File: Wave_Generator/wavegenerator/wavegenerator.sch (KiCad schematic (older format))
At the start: 59 parts, among them J1 01x05, J2 USB_B_Micro, J3 Conn_Coaxial, J4 1x2Pinheader, SW1 button, SW2 button, SW3 SP3T, U1 ATmega328P-AU, U101 AZ1117E-3.3, U102 MC33063AD, U2 MAX038CPP, Y101 16MHz

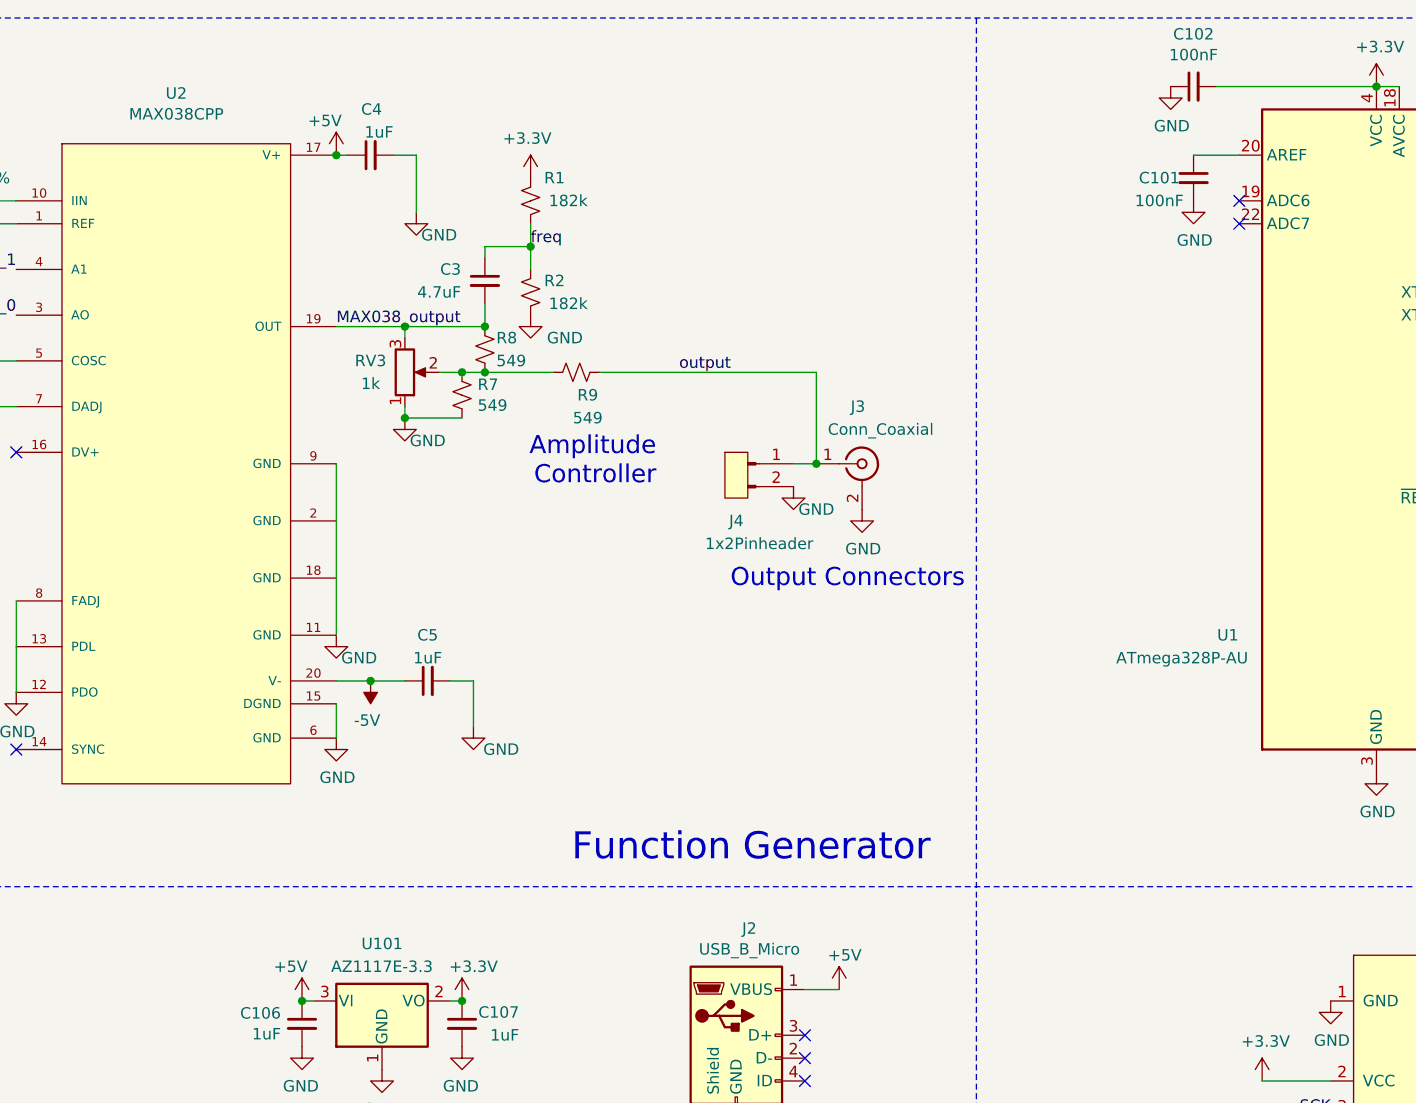
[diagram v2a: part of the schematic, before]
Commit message: oscilloscope instructions
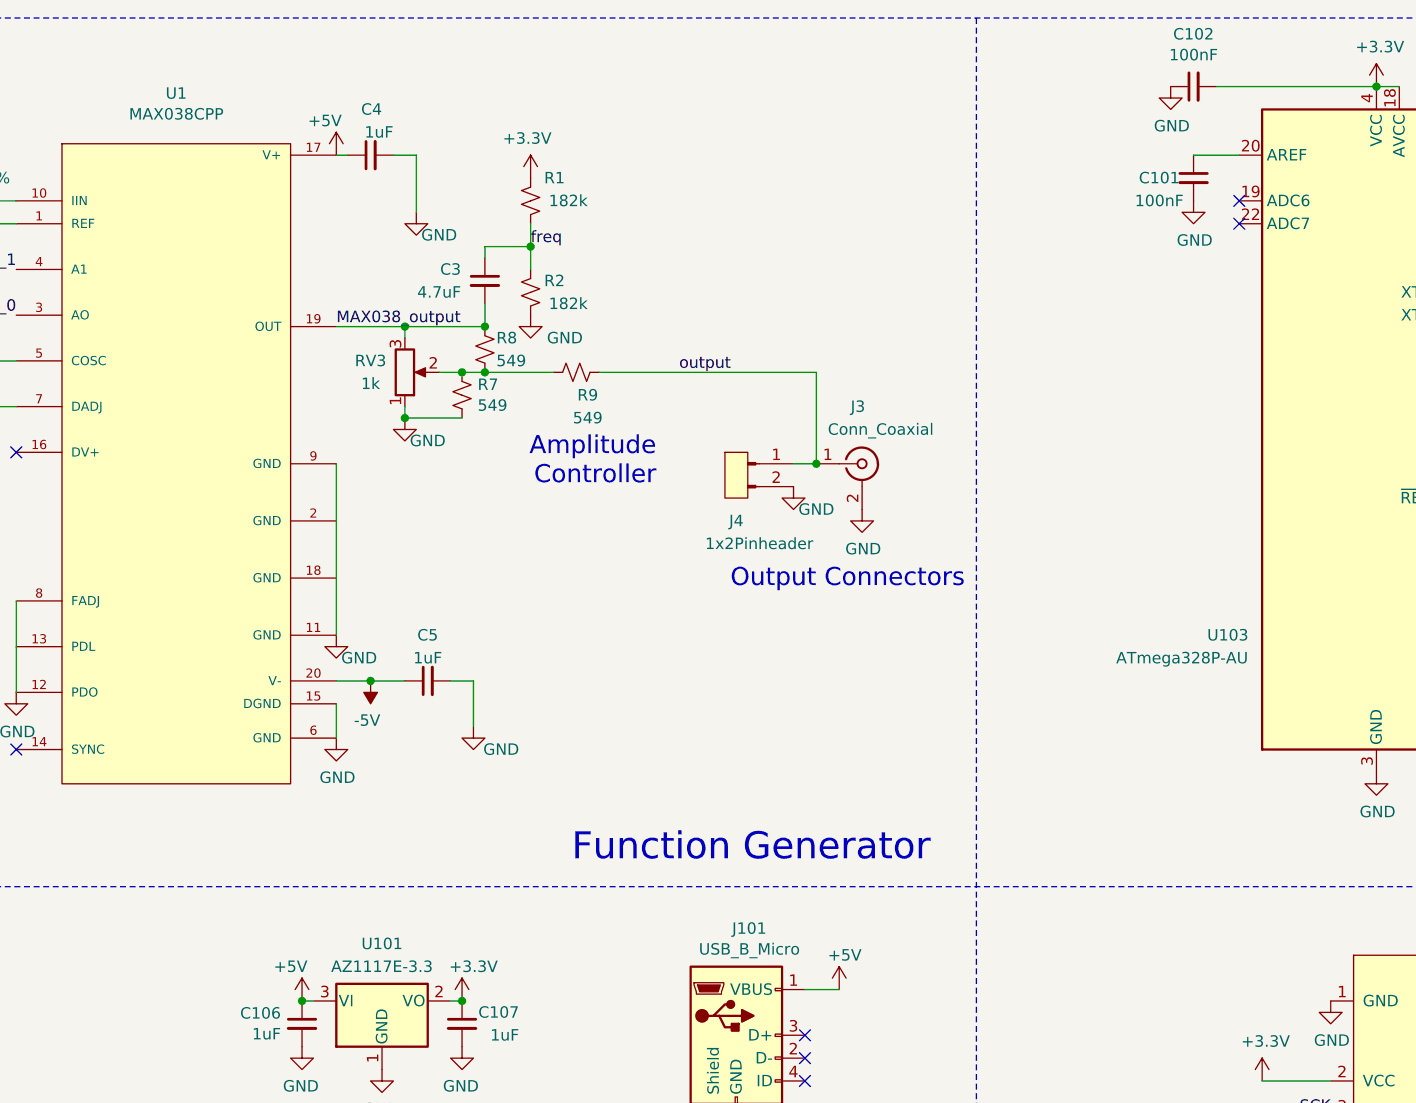
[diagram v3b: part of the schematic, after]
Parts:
- renumbered J2 to J101, U2 to U1, U1 to U103
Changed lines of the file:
@@
 $EndComp
 $Comp
-L Connector:USB_B_Micro J2
+L Connector:USB_B_Micro J101
 U 1 1 5D241E68
 P 5800 4950
-F 0 "J2" H 5857 5417 50  0000 C CNN
+F 0 "J101" H 5857 5417 50  0000 C CNN
 F 1 "USB_B_Micro" H 5857 5326 50  0000 C CNN
 F 2 "wavegenerator:USB_Micro-B_Amphenol_10118194-0001LF_Horizontal" H 5950 4900 50  0001 C CNN
@@
 $EndComp
 $Comp
-L wavegenerator:MAX038CPP U2
+L wavegenerator:MAX038CPP U1
 U 1 1 5D1E353F
 P 3350 2400
-F 0 "U2" H 3350 3970 50  0000 C CNN
+F 0 "U1" H 3350 3970 50  0000 C CNN
 F 1 "MAX038CPP" H 3350 3879 50  0000 C CNN
 F 2 "wavegenerator:MAX038CPP-W" H 3350 2400 50  0001 L BNN
@@
 	6100 4750 6250 4750
 $Comp
-L MCU_Microchip_ATmega:ATmega328P-AU U1
+L MCU_Microchip_ATmega:ATmega328P-AU U103
 U 1 1 5D258DD6
 P 8600 2300
-F 0 "U1" H 7950 1400 50  0000 C CNN
+F 0 "U103" H 7950 1400 50  0000 C CNN
 F 1 "ATmega328P-AU" H 7750 1300 50  0000 C CNN
 F 2 "Package_QFP:TQFP-32_7x7mm_P0.8mm" H 8600 2300 50  0001 C CIN
@@
 Text Label 9200 3300 0    50   ~ 0
 freq
-Connection ~ 4050 1100
 Wire Wire Line
 	4050 1100 4100 1100
